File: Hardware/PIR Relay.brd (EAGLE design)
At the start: 38.1 x 100.3 mm, 51 parts, among them J1 POWER_JACK, J2 3-PIN SMD, J4 AVR_SPI_PROG_3X22X3_LOCK, J5 RA 6Pin SMD, K1 RELAY-SPDT-JQX-15F, Q1 600mA/40V, U1 AP3012, U2 ATMEGA328P_TQFP

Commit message: Rerouted. Fixed header problem
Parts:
- removed J5: RA 6Pin SMD, SparkFun-Connectors:1X06-SMD_RA_MALE
- added J6: RA 6Pin SMD, SparkFun-Connectors:1X06-SMD_RA_MALE
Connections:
- net 5V: now also J6.4; no longer J5.3
- net CTS: now also J6.5; no longer J5.2
- net DTR: now also J6.1; no longer J5.6
- net GND: now also J6.6; no longer J5.1
- net PIR_#_ALARM: now also U2.25
- net RX: now also J6.2, U2.31; no longer J5.5, U2.30
- net TX: now also J6.3, U2.30; no longer J5.4, U2.31
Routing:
- net PIR_#_ALARM: track 21.1 -> 54.8 mm, vias 2 -> 3
- net DTR: track 40.7 -> 57.4 mm
- net 5V: track 137.2 -> 131.1 mm, vias 2 -> 4
- net RX: track 30.8 -> 36.1 mm
- net TX: track 33.6 -> 35.2 mm

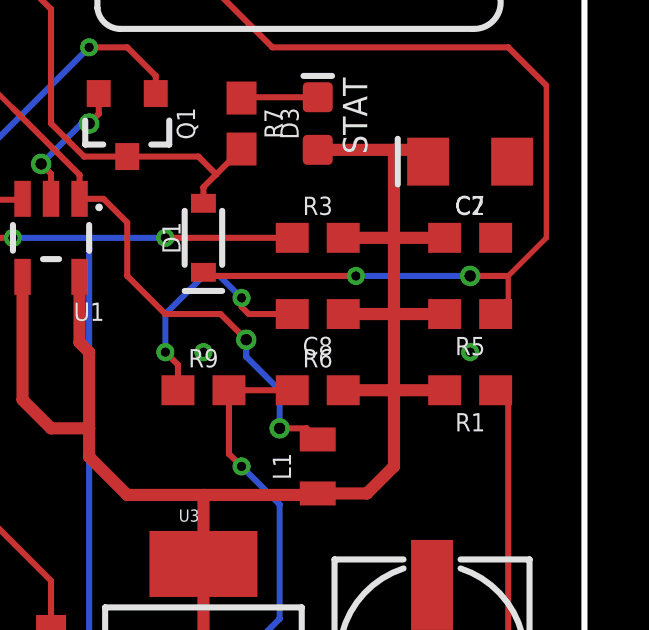
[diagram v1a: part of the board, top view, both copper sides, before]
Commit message: swapped 47k for 0hm
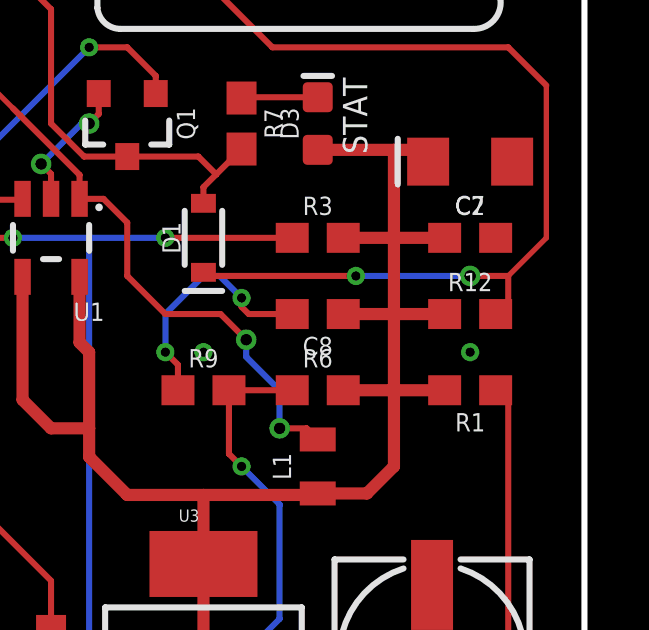
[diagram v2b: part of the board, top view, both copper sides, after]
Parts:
- R12: value 47k -> 0
- turned R12 to 0 degrees
- renumbered R5 to R12
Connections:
- net 5V: now also R12.1; no longer R12.2
- net N$8: now also R12.2; no longer R12.1
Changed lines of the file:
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@@
 <attribute name="VALUE" x="16.51" y="56.388" size="0.6096" layer="27" font="vector" ratio="20" align="top-center"/>
-</element>
-<element name="R5" library="SparkFun-Resistors" package="0603" value="47k" x="34.29" y="53.34" smashed="yes" rot="R180">
-<attribute name="NAME" x="34.29" y="52.578" size="0.6096" layer="25" font="vector" ratio="20" rot="R180" align="bottom-center"/>
-<attribute name="PROD_ID" value="RES-07871" x="-33.02" y="120.65" size="1.778" layer="27" rot="R180" display="off"/>
-<attribute name="VALUE" x="34.29" y="54.102" size="0.6096" layer="27" font="vector" ratio="20" rot="R180" align="top-center"/>
 </element>
 <element name="R6" library="SparkFun-Resistors" package="0603" value="240" x="29.21" y="50.8" smashed="yes">
@@
 <attribute name="PROD_ID" value="CONN-08971" x="1.27" y="33.02" size="1.778" layer="27" rot="R270" display="off"/>
 <attribute name="VALUE" x="0.254" y="34.671" size="0.6096" layer="27" font="vector" ratio="20" rot="R270"/>
+</element>
+<element name="R12" library="SparkFun-Resistors" package="0603" value="0" x="34.29" y="53.34" smashed="yes">
+<attribute name="NAME" x="34.29" y="54.102" size="0.6096" layer="25" font="vector" ratio="20" align="bottom-center"/>
+<attribute name="PROD_ID" value="RES-08609" x="34.29" y="53.34" size="1.778" layer="27" display="off"/>
+<attribute name="VALUE" x="34.29" y="52.578" size="0.6096" layer="27" font="vector" ratio="20" align="top-center"/>
 </element>
 </elements>
@@
 <signal name="N$8">
 <contactref element="D1" pad="C"/>
-<contactref element="R5" pad="1"/>
 <contactref element="K1" pad="COIL1"/>
 <wire x1="8.89" y1="82.48" x2="22.0894" y2="69.2806" width="0.2032" layer="1"/>
@@
 <via x="34.29" y="54.61" extent="1-16" drill="0.381"/>
 <wire x1="35.56" y1="54.61" x2="34.29" y2="54.61" width="0.2032" layer="1"/>
-<wire x1="35.56" y1="53.34" x2="35.14" y2="53.34" width="0.254" layer="1"/>
 <wire x1="36.83" y1="60.96" x2="36.83" y2="55.88" width="0.1778" layer="1"/>
 <wire x1="36.83" y1="55.88" x2="35.56" y2="54.61" width="0.1778" layer="1"/>
-<wire x1="35.14" y1="53.34" x2="35.56" y2="53.76" width="0.1778" layer="1"/>
-<wire x1="35.56" y1="53.76" x2="35.56" y2="54.61" width="0.1778" layer="1"/>
+<contactref element="R12" pad="2"/>
+<wire x1="35.56" y1="54.61" x2="35.56" y2="53.34" width="0.2032" layer="1"/>
+<wire x1="35.56" y1="53.34" x2="35.14" y2="53.34" width="0.2032" layer="1"/>
 </signal>
 <signal name="N$9">
@@
 <contactref element="U2" pad="18"/>
 <contactref element="J4" pad="2"/>
-<contactref element="R5" pad="2"/>
 <contactref element="D3" pad="A"/>
 <contactref element="R3" pad="2"/>
@@
 <wire x1="14.7574" y1="20.72" x2="16.11" y2="20.72" width="0.2032" layer="1"/>
 <wire x1="16.11" y1="20.72" x2="17.71" y2="19.12" width="0.2032" layer="1"/>
-<wire x1="31.75" y1="53.34" x2="33.44" y2="53.34" width="0.4064" layer="1"/>
 <wire x1="33.44" y1="50.8" x2="31.75" y2="50.8" width="0.4064" layer="1"/>
 <wire x1="25.4" y1="38.8112" x2="25.4" y2="35.56" width="0.4064" layer="1"/>
@@
 <via x="10.16" y="24.13" extent="1-16" drill="0.35"/>
 <wire x1="10.16" y1="24.13" x2="10.16" y2="22.86" width="0.2032" layer="1"/>
+<contactref element="R12" pad="1"/>
+<wire x1="33.44" y1="53.34" x2="31.75" y2="53.34" width="0.4064" layer="1"/>
 </signal>
 <signal name="N$13">

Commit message: v02
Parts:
- moved J6 1.27 mm to (1.27, 31.8)
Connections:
- net RX renamed FTDI-RX
- net TX renamed FTDI-TX
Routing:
- net GND: track 50.8 -> 45.3 mm, vias 15 -> 17
- net 5V: track 131.1 -> 129.9 mm
- net FTDI-RX: track 36.1 -> 35.4 mm
- net DTR: track 57.4 -> 57.9 mm
- net FTDI-TX: track 35.2 -> 34.6 mm
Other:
- board text added: "2/18/2021"
- board text added: "BLK"
- board text added: "GRN"
- board text added: "v02"
- board text removed: "12/3/2020"
